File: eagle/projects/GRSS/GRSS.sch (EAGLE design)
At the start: 37 parts, among them J1 MOL-SL-2-RA, J10 MOL-SL-2-RA, J11 MOL-SL-2-RA, J2 MOL-SL-2-RA, J3 MOL-SL-2-RA, J4 MOL-SL-2-RA, J5 MOL-SL-2-RA, J6 MOL-SL-2-RA, J7 MOL-SL-2-RA, J8 MOL-SL-2-RA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

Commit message: Turned one connector to vertical
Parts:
- J11: value MOL-SL-2-RA -> MOL-SL-2-V; device grss:MOLSL_2PIN_SL2RA_RA -> grss:MOLSL_2PIN_SL2V_V
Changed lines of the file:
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@@
 <part name="C1" library="grss" deviceset="CAP" device="_0805" technology="_1UF0" value="1uF"/>
 <part name="C5" library="grss" deviceset="CAP" device="_0805" technology="_10NF0" value="0.01uF"/>
-<part name="J11" library="grss" deviceset="MOLSL_2PIN" device="_RA" technology="_SL2RA" value="MOL-SL-2-RA"/>
+<part name="J11" library="grss" deviceset="MOLSL_2PIN" device="_V" technology="_SL2V" value="MOL-SL-2-V"/>
 <part name="FRAME1" library="frames" deviceset="A4L-LOC" device="" value="Schematic"/>
 <part name="U2" library="grss" deviceset="LMC555CMX/NOPB" device="" value="LMC555CMX/NOPB"/>
@@
 <instance part="J11" gate="G$1" x="-185.42" y="154.94" smashed="yes">
 <attribute name="NAME" x="-190.5" y="162.56" size="2.0828" layer="95" align="center-left"/>
-<attribute name="VALUE" x="-183.896" y="147.32" size="1.778" layer="96" align="center"/>
+<attribute name="VALUE" x="-183.134" y="147.32" size="1.778" layer="96" align="center"/>
 </instance>
 <instance part="FRAME1" gate="G$1" x="-195.58" y="48.26"/>

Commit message: tNames Aestetics
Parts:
- U2: value LMC555CMX/NOPB -> LMC555CMX
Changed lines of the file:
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@@
 <part name="J11" library="grss" deviceset="MOLSL_2PIN" device="_V" technology="_SL2V" value="MOL-SL-2-V"/>
 <part name="FRAME1" library="frames" deviceset="A4L-LOC" device="" value="Schematic"/>
-<part name="U2" library="grss" deviceset="LMC555CMX/NOPB" device="" value="LMC555CMX/NOPB"/>
+<part name="U2" library="grss" deviceset="LMC555CMX/NOPB" device="" value="LMC555CMX"/>
 <part name="U1" library="grss" deviceset="LP2985AIM5-4.5/NOPB" device="" value="LP2985AIM5-4.5/NOPB"/>
 <part name="Q1" library="grss" deviceset="STD12NF06LT4" device="" value="STD12NF06LT4"/>

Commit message: updated FET, LDO, 555 Timer for dots / silkscreen
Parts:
- U2: value LMC555CMX -> LMC555CMX/NOPB
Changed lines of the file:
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@@
 <part name="J11" library="grss" deviceset="MOLSL_2PIN" device="_V" technology="_SL2V" value="MOL-SL-2-V"/>
 <part name="FRAME1" library="frames" deviceset="A4L-LOC" device="" value="Schematic"/>
-<part name="U2" library="grss" deviceset="LMC555CMX/NOPB" device="" value="LMC555CMX"/>
+<part name="U2" library="grss" deviceset="LMC555CMX/NOPB" device="" value="LMC555CMX/NOPB"/>
 <part name="U1" library="grss" deviceset="LP2985AIM5-4.5/NOPB" device="" value="LP2985AIM5-4.5/NOPB"/>
 <part name="Q1" library="grss" deviceset="STD12NF06LT4" device="" value="STD12NF06LT4"/>

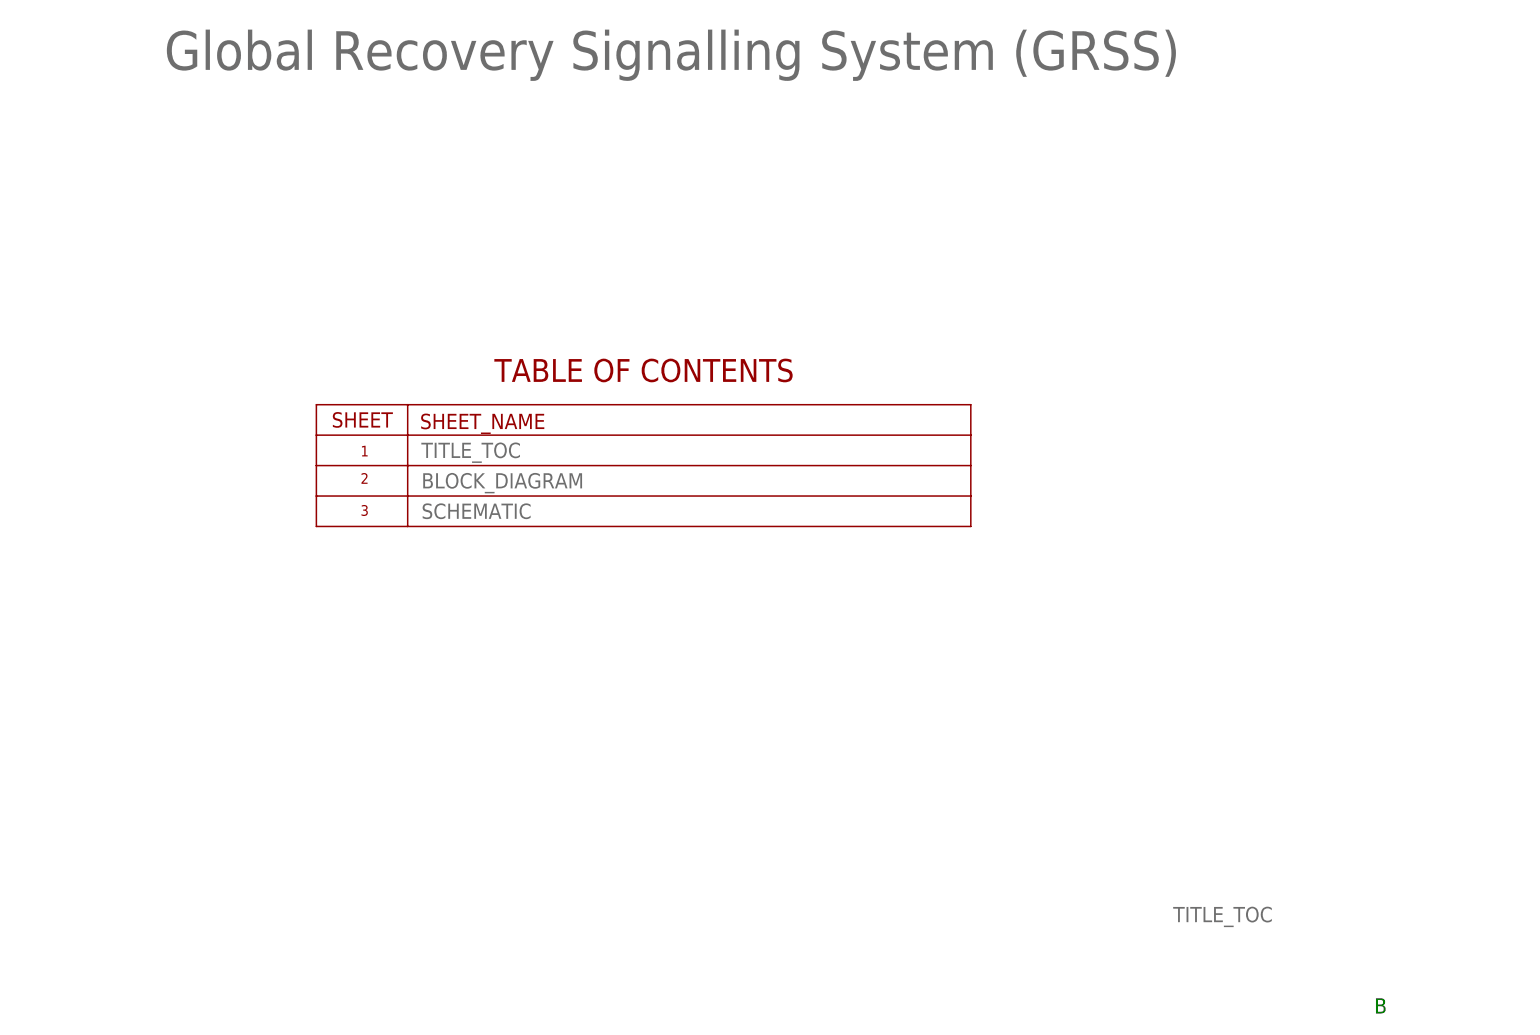
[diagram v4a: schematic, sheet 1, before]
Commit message: Added Squad Logo
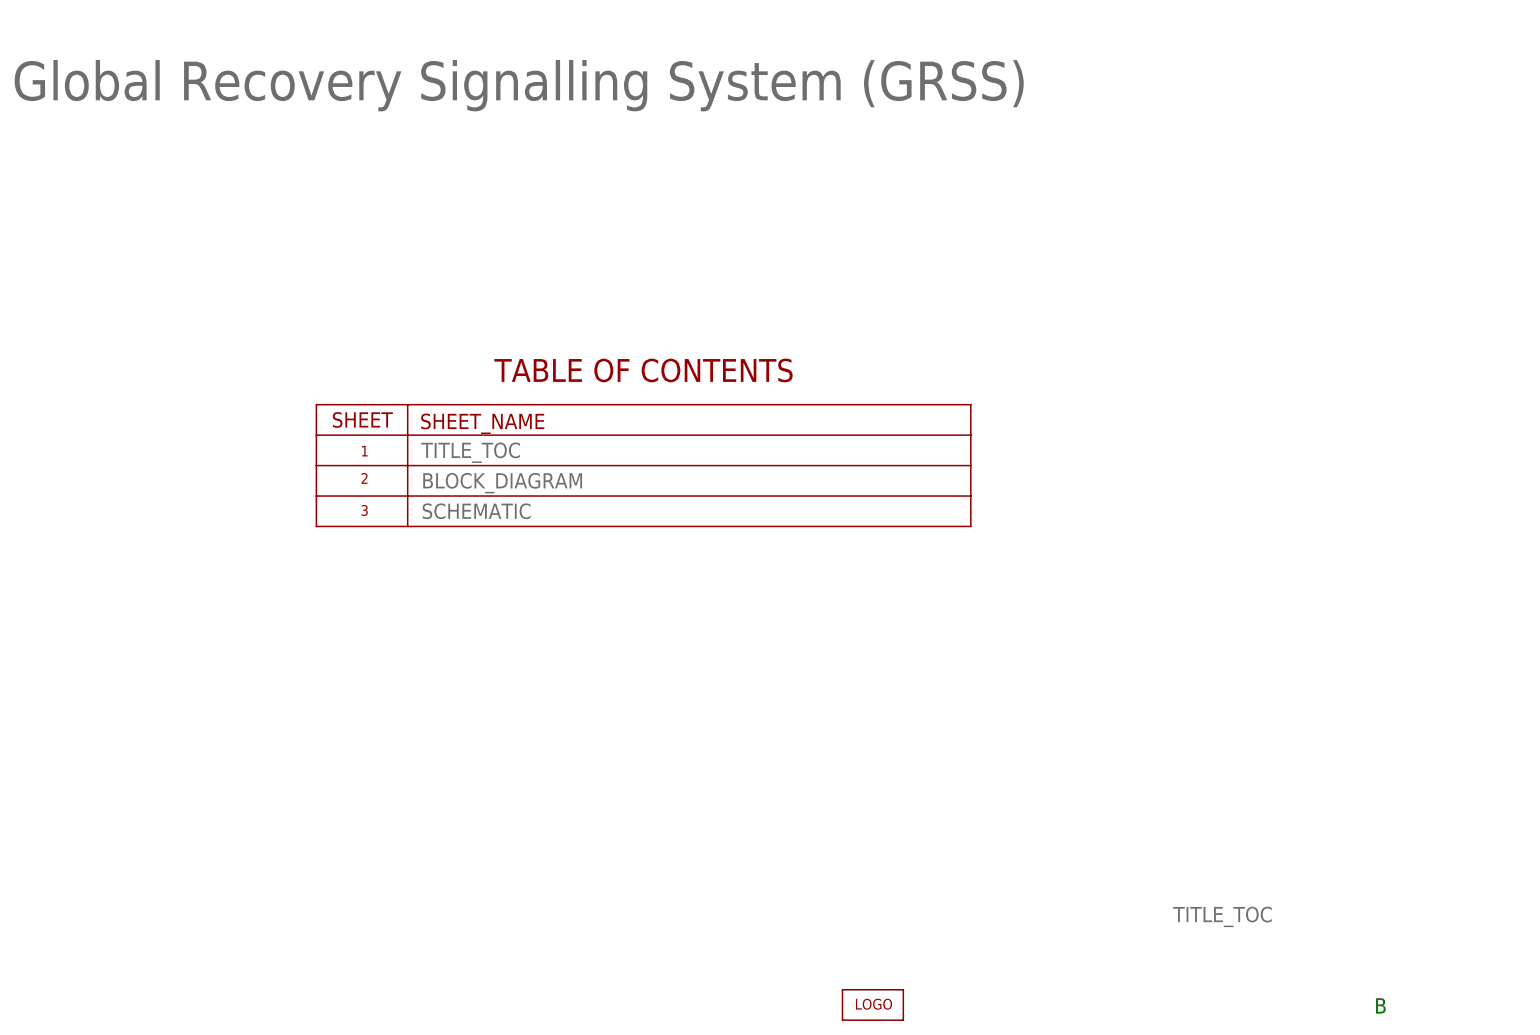
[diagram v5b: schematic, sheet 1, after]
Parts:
- added IMAGE1: SQUAD_LOGO, grss:SQUAD_LOGO
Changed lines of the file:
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@@
 <setting verticaltext="up"/>
 </settings>
-<grid distance="0.1" unitdist="inch" unit="inch" style="lines" multiple="1" display="no" altdistance="0.01" altunitdist="inch" altunit="inch"/>
+<grid distance="0.1" unitdist="mm" unit="mm" style="lines" multiple="1" display="no" altdistance="0.01" altunitdist="mm" altunit="mm"/>
 <layers>
 <layer number="1" name="Top" color="4" fill="1" visible="no" active="no"/>
@@
 <part name="C3" library="grss" deviceset="CAP" device="_0805" technology="_1UF0" value="1uF"/>
 <part name="R7" library="grss" deviceset="RES" device="_0805" technology="_0R0" value="0.0"/>
+<part name="IMAGE1" library="grss" deviceset="SQUAD_LOGO" device=""/>
 </parts>
 <sheets>
@@
 <text x="65.786" y="85.09" size="2.54" layer="95">BLOCK_DIAGRAM</text>
 <text x="65.786" y="80.01" size="2.54" layer="95">SCHEMATIC</text>
-<text x="22.86" y="154.94" size="6.4516" layer="95">Global Recovery Signalling System (GRSS)</text>
+<text x="-2.54" y="149.86" size="6.4516" layer="95">Global Recovery Signalling System (GRSS)</text>
 <text x="191.262" y="12.7" size="2.54" layer="95">TITLE_TOC</text>
 <text x="224.79" y="-2.54" size="2.54" layer="91">B</text>
@@
 <instance part="FRAME2" gate="G$1" x="-25.4" y="-7.62"/>
 <instance part="U$1" gate="G$1" x="66.04" y="93.98"/>
+<instance part="IMAGE1" gate="G$1" x="141.14" y="-1.12"/>
 </instances>
 <busses>

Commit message: Squad Logo / 2-layer
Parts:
- removed IMAGE1: SQUAD_LOGO, grss:SQUAD_LOGO
- added LOGO1: (no value), grss:SQUAD_LOGO
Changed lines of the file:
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@@
 <setting verticaltext="up"/>
 </settings>
-<grid distance="0.1" unitdist="mm" unit="mm" style="lines" multiple="1" display="no" altdistance="0.01" altunitdist="mm" altunit="mm"/>
+<grid distance="0.1" unitdist="inch" unit="inch" style="lines" multiple="1" display="no" altdistance="0.01" altunitdist="inch" altunit="inch"/>
 <layers>
 <layer number="1" name="Top" color="4" fill="1" visible="no" active="no"/>
@@
 <part name="C3" library="grss" deviceset="CAP" device="_0805" technology="_1UF0" value="1uF"/>
 <part name="R7" library="grss" deviceset="RES" device="_0805" technology="_0R0" value="0.0"/>
-<part name="IMAGE1" library="grss" deviceset="SQUAD_LOGO" device=""/>
+<part name="LOGO1" library="grss" deviceset="SQUAD_LOGO" device=""/>
 </parts>
 <sheets>
@@
 <instance part="FRAME2" gate="G$1" x="-25.4" y="-7.62"/>
 <instance part="U$1" gate="G$1" x="66.04" y="93.98"/>
-<instance part="IMAGE1" gate="G$1" x="141.14" y="-1.12"/>
+<instance part="LOGO1" gate="G$1" x="138.938" y="-0.762"/>
 </instances>
 <busses>

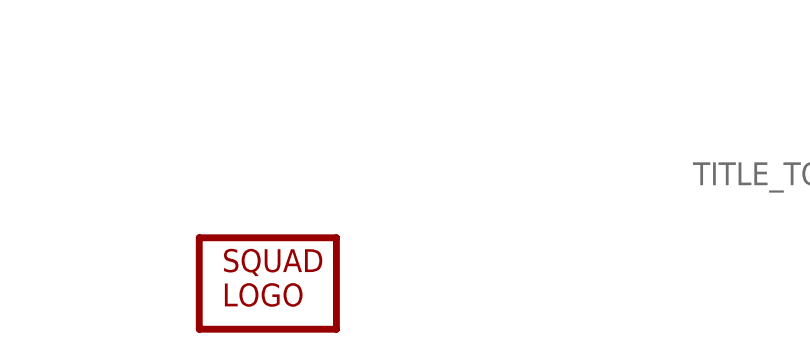
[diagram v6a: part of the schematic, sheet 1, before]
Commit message: GND / Power Planes - LG
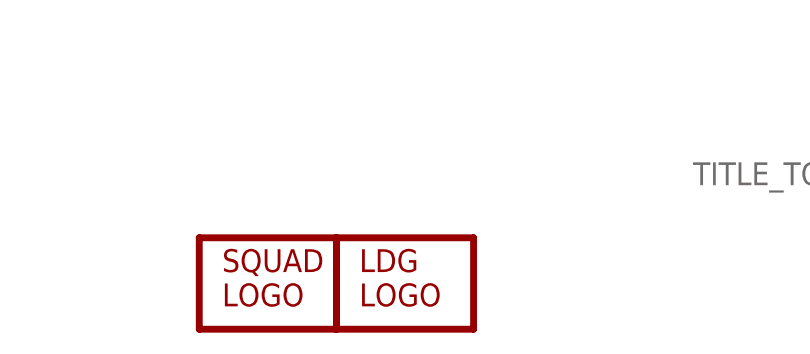
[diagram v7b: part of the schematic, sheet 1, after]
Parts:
- added U$3: LG, grss:LG
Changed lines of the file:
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@@
 <part name="R7" library="grss" deviceset="RES" device="_0805" technology="_0R0" value="0.0"/>
 <part name="LOGO1" library="grss" deviceset="SQUAD_LOGO" device=""/>
+<part name="U$3" library="grss" deviceset="LG" device=""/>
 </parts>
 <sheets>
@@
 <instance part="U$1" gate="G$1" x="66.04" y="93.98"/>
 <instance part="LOGO1" gate="G$1" x="138.938" y="-0.762"/>
+<instance part="U$3" gate="G$1" x="154.178" y="-0.762"/>
 </instances>
 <busses>

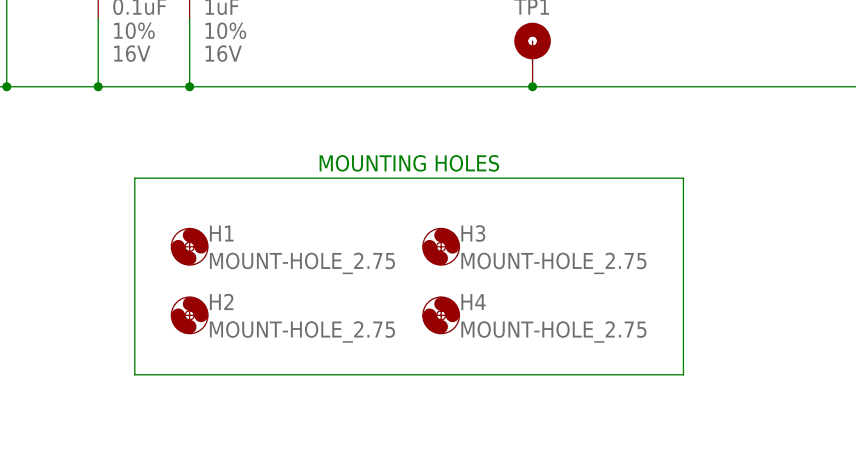
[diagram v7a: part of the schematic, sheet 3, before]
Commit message: moved mounting holes briefly
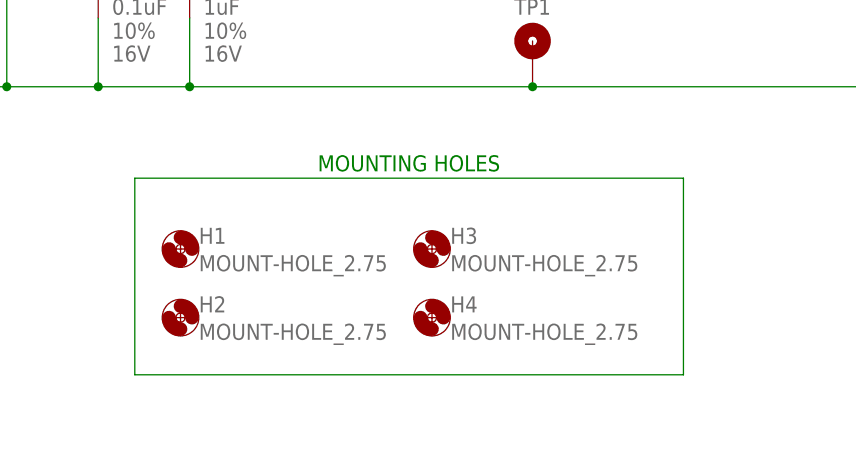
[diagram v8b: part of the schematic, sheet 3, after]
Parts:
- removed U$3: LG, grss:LG
- LOGO1: value (none) -> LOGO
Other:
- moved on the sheet: H1, H2, H3, H4
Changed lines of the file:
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@@
 <part name="TP3" library="grss" deviceset="TEST_POINT" device="_10R_SMD" technology="_TP10R_SMD" value="555OUT"/>
 <part name="TP4" library="grss" deviceset="TEST_POINT" device="_10R_SMD" technology="_TP10R_SMD" value="VD"/>
-<part name="H1" library="grss" deviceset="MOUNT-HOLE" device="_2.75"/>
-<part name="H2" library="grss" deviceset="MOUNT-HOLE" device="_2.75"/>
-<part name="H3" library="grss" deviceset="MOUNT-HOLE" device="_2.75"/>
-<part name="H4" library="grss" deviceset="MOUNT-HOLE" device="_2.75"/>
 <part name="U$2" library="grss" deviceset="BLOCK_DIAGRAM" device=""/>
 <part name="R3" library="grss" deviceset="RES" device="_0805" technology="_47R0" value="4.7k"/>
@@
 <part name="C3" library="grss" deviceset="CAP" device="_0805" technology="_1UF0" value="1uF"/>
 <part name="R7" library="grss" deviceset="RES" device="_0805" technology="_0R0" value="0.0"/>
-<part name="LOGO1" library="grss" deviceset="SQUAD_LOGO" device=""/>
-<part name="U$3" library="grss" deviceset="LG" device=""/>
+<part name="LOGO1" library="grss" deviceset="SQUAD_LOGO" device="" value="LOGO"/>
+<part name="H1" library="grss" deviceset="MOUNT-HOLE" device="_2.75"/>
+<part name="H2" library="grss" deviceset="MOUNT-HOLE" device="_2.75"/>
+<part name="H3" library="grss" deviceset="MOUNT-HOLE" device="_2.75"/>
+<part name="H4" library="grss" deviceset="MOUNT-HOLE" device="_2.75"/>
 </parts>
 <sheets>
@@
 <instance part="U$1" gate="G$1" x="66.04" y="93.98"/>
 <instance part="LOGO1" gate="G$1" x="138.938" y="-0.762"/>
-<instance part="U$3" gate="G$1" x="154.178" y="-0.762"/>
 </instances>
 <busses>
@@
 <instance part="TP3" gate="G$1" x="-38.1" y="113.284"/>
 <instance part="TP4" gate="G$1" x="-5.08" y="119.38"/>
-<instance part="H1" gate="G$1" x="-144.78" y="73.66"/>
-<instance part="H2" gate="G$1" x="-144.78" y="66.04"/>
-<instance part="H3" gate="G$1" x="-116.84" y="73.66"/>
-<instance part="H4" gate="G$1" x="-116.84" y="66.04"/>
 <instance part="R3" gate="G$1" x="-32.766" y="97.79" rot="R90"/>
 <instance part="TP1" gate="G$1" x="-106.68" y="96.52"/>
@@
 <instance part="C3" gate="G$1" x="-144.78" y="101.6"/>
 <instance part="R7" gate="G$1" x="-20.32" y="97.79" rot="R90"/>
+<instance part="H1" gate="G$1" x="-145.796" y="73.406"/>
+<instance part="H2" gate="G$1" x="-145.796" y="65.786"/>
+<instance part="H3" gate="G$1" x="-117.856" y="73.406"/>
+<instance part="H4" gate="G$1" x="-117.856" y="65.786"/>
 </instances>
 <busses>
